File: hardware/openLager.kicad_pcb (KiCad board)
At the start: 4 copper layers, 15.2 x 19 mm, 29 parts, among them J1 CONN_01X06, J2 DM3CS-SF, U1 STM32F411CEUx, U2 SPX3819M5-L-3-3, Y1 CSTCE8M00G15L99

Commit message: Minor tweaks as per @mlyle review
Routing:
- net GND: track 80.0 -> 91.5 mm
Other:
- board text added: "5V"
- board text added: "GND"
- board text added: "NRST"
- board text added: "RX/CK"
- board text added: "SI"
- board text added: "SO"
- board text added: "TX/CS"
- board text added: "openLager Rev A ©2016 dRonin - CC BY"
- board text removed: "openLager Rev A dRonin - CC BY"

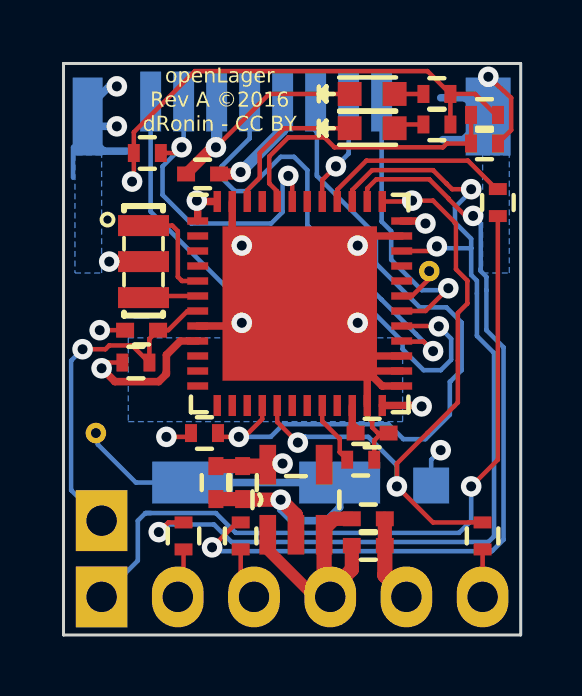
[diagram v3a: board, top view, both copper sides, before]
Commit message: DFM changes and added SS RefDes
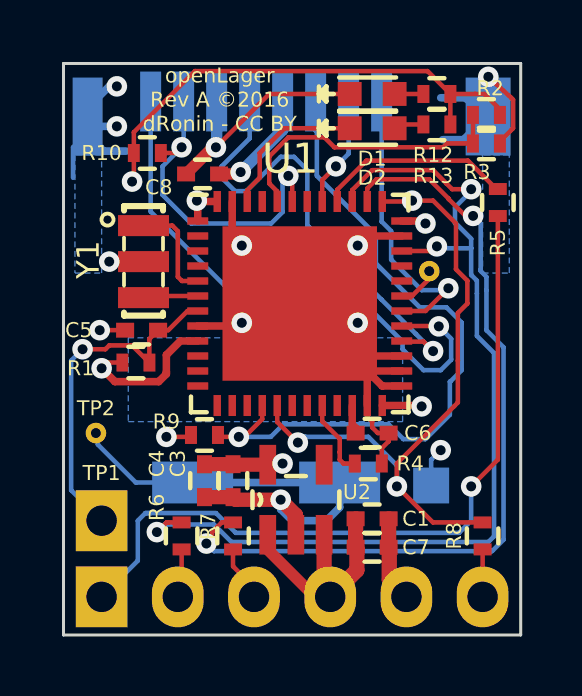
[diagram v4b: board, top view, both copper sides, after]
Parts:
- moved C4 0.39 mm to (195.2, 110.4)
- moved C3 0.32 mm to (196.2, 110.4)
- moved R4 0.28 mm to (200.7, 109.9)
- moved R7 0.25 mm to (196.2, 112.3)
- moved C7 0.14 mm to (200.8, 112.6)
- moved C1 0.13 mm to (200.8, 111.7)
- moved R2 0.06 mm to (204.6, 98.2)
- moved R3 0.06 mm to (204.6, 99.2)
- moved R9 0.06 mm to (195.2, 108.9)
- moved R6 0.06 mm to (194.4, 112.3)
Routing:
- net Net-(J1-Pad3): track 2.48 -> 1.87 mm
- net +3V3: track 31.8 -> 32.4 mm
- net GND: track 91.5 -> 92.1 mm

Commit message: Put dRonin logo on board (#42)
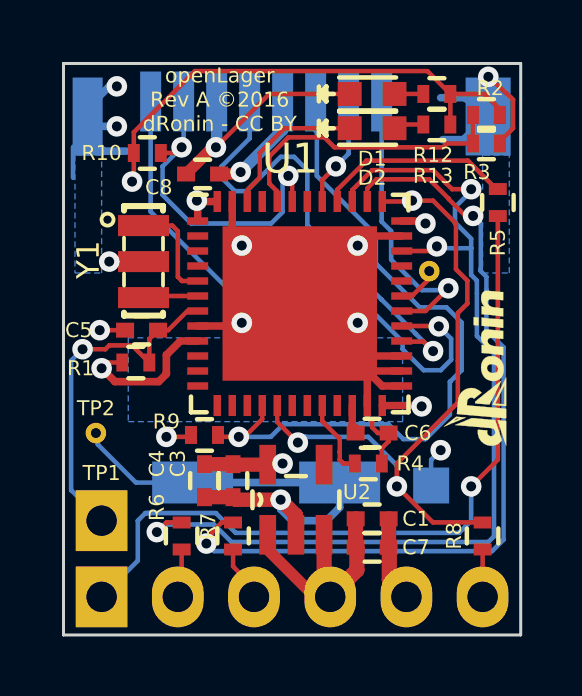
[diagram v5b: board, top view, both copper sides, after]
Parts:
- added G***: LOGO, dRLogo:test, F.Cu at (204.2, 106.7)

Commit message: Hardware rev b (#50)
* Updated to RevB, changed LED and SS

* Adding new BOM

* Changing SCH rev

* Change /NRST from pin to TP
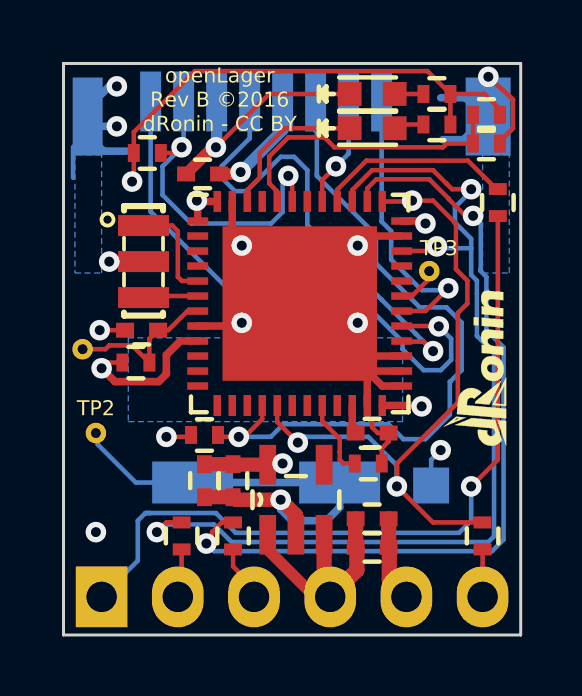
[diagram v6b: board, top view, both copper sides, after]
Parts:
- D1: value APHHS1005CGCK -> LG L29K-F2J1-24
- D2: value APHHS1005SURCK -> LS L29K-G1J2-1-Z
- TP1: footprint openLagerFootprints:Socket_Strip_Straight_1x01 -> openLagerFootprints:TP
- moved TP1 5.75 mm to (191.1, 106.0)
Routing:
- net NRST: track 12.7 -> 5.30 mm, vias 1 -> 0
- net GND: vias 12 -> 13
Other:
- board text added: "openLager Rev B ©2016 dRonin - CC BY"
- board text removed: "NRST"
- board text removed: "openLager Rev A ©2016 dRonin - CC BY"

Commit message: Add (very simple) fab drawing to openlager. (#51)
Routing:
- net GND: vias 13 -> 12
- net (no net): vias 0 -> 1
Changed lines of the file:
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@@
     (area 186.709267 94.1961 208.776305 121.981539)
     (thickness 1.6)
-    (drawings 12)
+    (drawings 16)
     (tracks 428)
     (zones 0)
@@
     (1 In1.Cu power hide)
     (2 In2.Cu power hide)
-    (31 B.Cu signal)
+    (31 B.Cu signal hide)
     (34 B.Paste user hide)
     (35 F.Paste user hide)
-    (36 B.SilkS user)
-    (37 F.SilkS user)
+    (36 B.SilkS user hide)
+    (37 F.SilkS user hide)
     (38 B.Mask user hide)
     (39 F.Mask user hide)
     (40 Dwgs.User user hide)
-    (44 Edge.Cuts user)
+    (44 Edge.Cuts user hide)
+    (49 F.Fab user)
   )
   (setup
@@
     (pcb_text_size 1.5 1.5)
     (mod_edge_width 0.15)
-    (mod_text_size 1 1)
-    (mod_text_width 0.15)
+    (mod_text_size 0.5 0.5)
+    (mod_text_width 0.125)
     (pad_size 2.2352 2.2352)
     (pad_drill 1.016)
@@
     (pad_to_paste_clearance_ratio -0.1)
     (aux_axis_origin 0 0)
-    (visible_elements 7FFFFF5F)
+    (visible_elements 7FFFFB3F)
     (pcbplotparams
       (layerselection 0x010fc_80000007)
@@
     (tags "capacitor 0402")
     (attr smd)
-    (fp_text reference C1 (at 1.4605 0) (layer F.SilkS) hide
+    (fp_text reference C1 (at 0 0) (layer F.Fab)
       (effects (font (size 0.5 0.5) (thickness 0.125)))
     )
@@
     (tags "capacitor 0402")
     (attr smd)
-    (fp_text reference C3 (at -0.5715 1.8415 270) (layer F.SilkS) hide
+    (fp_text reference C3 (at 0 0 270) (layer F.Fab)
       (effects (font (size 0.5 0.5) (thickness 0.125)))
     )
@@
     (tags "capacitor 0402")
     (attr smd)
-    (fp_text reference C4 (at -0.5715 1.5875 270) (layer F.SilkS) hide
+    (fp_text reference C4 (at 0 0 270) (layer F.Fab)
       (effects (font (size 0.5 0.5) (thickness 0.125)))
     )
@@
     (tags "capacitor 0402")
     (attr smd)
-    (fp_text reference C5 (at 2.0955 0 180) (layer F.SilkS) hide
+    (fp_text reference C5 (at 0 0 180) (layer F.Fab)
       (effects (font (size 0.5 0.5) (thickness 0.125)))
     )
@@
     (tags "capacitor 0402")
     (attr smd)
-    (fp_text reference C6 (at 1.524 0) (layer F.SilkS) hide
+    (fp_text reference C6 (at 0 0) (layer F.Fab)
       (effects (font (size 0.5 0.5) (thickness 0.125)))
     )
@@
     (tags "capacitor 0402")
     (attr smd)
-    (fp_text reference C7 (at 1.4605 0) (layer F.SilkS) hide
+    (fp_text reference C7 (at 0 0) (layer F.Fab)
       (effects (font (size 0.5 0.5) (thickness 0.125)))
     )
@@
     (tags "capacitor 0402")
     (attr smd)
-    (fp_text reference C8 (at 1.4605 -0.4445 180) (layer F.SilkS) hide
+    (fp_text reference C8 (at 0 0 180) (layer F.Fab)
       (effects (font (size 0.5 0.5) (thickness 0.125)))
     )
@@
     (attr smd)
     (fp_text reference J2 (at 1.524 -13.335) (layer B.SilkS) hide
-      (effects (font (size 1 1) (thickness 0.15)) (justify mirror))
+      (effects (font (size 0.5 0.5) (thickness 0.125)) (justify mirror))
     )
     (fp_text value DM3CS-SF (at -7.025 -16.065) (layer B.SilkS) hide
@@
     (tags "resistor 0402")
     (attr smd)
-    (fp_text reference R1 (at -1.8415 0.1905) (layer F.SilkS) hide
+    (fp_text reference R1 (at 0 0) (layer F.Fab)
       (effects (font (size 0.5 0.5) (thickness 0.125)))
     )
@@
     (tags "resistor 0402")
     (attr smd)
-    (fp_text reference R2 (at -0.127 0.889 180) (layer F.SilkS) hide
+    (fp_text reference R2 (at 0 0 180) (layer F.Fab)
       (effects (font (size 0.5 0.5) (thickness 0.125)))
     )
@@
     (tags "resistor 0402")
     (attr smd)
-    (fp_text reference R3 (at -0.3175 0.9525) (layer F.SilkS) hide
+    (fp_text reference R3 (at 0 0) (layer F.Fab)
       (effects (font (size 0.5 0.5) (thickness 0.125)))
     )
@@
     (tags "resistor 0402")
     (attr smd)
-    (fp_text reference R4 (at 1.397 0) (layer F.SilkS) hide
+    (fp_text reference R4 (at 0 0) (layer F.Fab)
       (effects (font (size 0.5 0.5) (thickness 0.125)))
     )
@@
     (tags "resistor 0402")
     (attr smd)
-    (fp_text reference R5 (at -1.3335 0 90) (layer F.SilkS) hide
+    (fp_text reference R5 (at 0 0 90) (layer F.Fab)
       (effects (font (size 0.5 0.5) (thickness 0.125)))
     )
@@
     (tags "resistor 0402")
     (attr smd)
-    (fp_text reference R6 (at 0.9525 -0.8255 90) (layer F.SilkS) hide
+    (fp_text reference R6 (at 0 0 90) (layer F.Fab)
       (effects (font (size 0.5 0.5) (thickness 0.125)))
     )
@@
     (tags "resistor 0402")
     (attr smd)
-    (fp_text reference R7 (at 0.3175 -0.8255 90) (layer F.SilkS) hide
+    (fp_text reference R7 (at 0 0 90) (layer F.Fab)
       (effects (font (size 0.5 0.5) (thickness 0.125)))
     )
@@
     (tags "resistor 0402")
     (attr smd)
-    (fp_text reference R8 (at 0 -0.9525 90) (layer F.SilkS) hide
+    (fp_text reference R8 (at 0 0 90) (layer F.Fab)
       (effects (font (size 0.5 0.5) (thickness 0.125)))
     )
@@
     (tags "resistor 0402")
     (attr smd)
-    (fp_text reference R9 (at -1.27 -0.4445) (layer F.SilkS) hide
+    (fp_text reference R9 (at 0 0) (layer F.Fab)
       (effects (font (size 0.5 0.5) (thickness 0.125)))
     )
@@
     (tags "resistor 0402")
     (attr smd)
-    (fp_text reference R10 (at -1.524 0) (layer F.SilkS) hide
+    (fp_text reference R10 (at 0 0) (layer F.Fab)
       (effects (font (size 0.5 0.5) (thickness 0.125)))
     )
@@
     (tags "resistor 0402")
     (attr smd)
-    (fp_text reference R12 (at -0.127 2.032) (layer F.SilkS) hide
+    (fp_text reference R12 (at 0 0) (layer F.Fab)
       (effects (font (size 0.5 0.5) (thickness 0.125)))
     )
@@
     (tags "resistor 0402")
     (attr smd)
-    (fp_text reference R13 (at 0.127 -1.7145 180) (layer F.SilkS) hide
+    (fp_text reference R13 (at 0 0 180) (layer F.Fab)
       (effects (font (size 0.5 0.5) (thickness 0.125)))
     )
@@
     (tags "QFN 0.5")
     (attr smd)
-    (fp_text reference U1 (at -0.3175 -4.826) (layer F.SilkS) hide
-      (effects (font (size 1 1) (thickness 0.15)))
+    (fp_text reference U1 (at 0 0) (layer F.Fab)
+      (effects (font (size 0.5 0.5) (thickness 0.125)))
     )
     (fp_text value STM32F411CEUx (at 0 4.75) (layer F.Fab) hide
@@
     (solder_mask_margin 0.1)
     (attr smd)
-    (fp_text reference Y1 (at -0.0635 1.8415 270) (layer F.SilkS) hide
-      (effects (font (size 0.75 0.75) (thickness 0.1)))
+    (fp_text reference Y1 (at 0 0 270) (layer F.Fab)
+      (effects (font (size 0.5 0.5) (thickness 0.125)))
     )
     (fp_text value CSTCE8M00G15L99 (at 0.3175 1.8875 270) (layer F.SilkS) hide
@@
     (tags "socket strip")
     (fp_text reference J1 (at 0 -5.1) (layer F.SilkS) hide
-      (effects (font (size 1 1) (thickness 0.15)))
+      (effects (font (size 0.5 0.5) (thickness 0.125)))
     )
     (fp_text value CONN_01X06 (at 0 -3.1) (layer F.Fab) hide
@@
     (tags "LED led 0603 SMD smd SMT smt smdled SMDLED smtled SMTLED")
     (attr smd)
-    (fp_text reference D1 (at 0 2.159) (layer F.SilkS) hide
+    (fp_text reference D1 (at 0 0) (layer F.Fab)
       (effects (font (size 0.5 0.5) (thickness 0.125)))
     )
@@
     (tags "LED led 0603 SMD smd SMT smt smdled SMDLED smtled SMTLED")
     (attr smd)
-    (fp_text reference D2 (at 0 1.651) (layer F.SilkS) hide
+    (fp_text reference D2 (at 0 0) (layer F.Fab)
       (effects (font (size 0.5 0.5) (thickness 0.125)))
     )
@@
     (solder_mask_margin 0.1)
     (attr smd)
-    (fp_text reference U2 (at 0.254 2.032 180) (layer F.SilkS) hide
+    (fp_text reference U2 (at 0 0 180) (layer F.Fab)
       (effects (font (size 0.5 0.5) (thickness 0.125)))
     )
@@
     (at 204.216 106.68 90)
     (fp_text reference G*** (at 0 0 90) (layer F.SilkS) hide
-      (effects (font (thickness 0.3)))
+      (effects (font (size 0.5 0.5) (thickness 0.125)))
     )
     (fp_text value LOGO (at 0.75 0 90) (layer F.SilkS) hide
@@
     (at 191.135 106.045)
     (fp_text reference TP1 (at 0 0.5) (layer F.SilkS) hide
-      (effects (font (size 1 1) (thickness 0.15)))
+      (effects (font (size 0.5 0.5) (thickness 0.125)))
     )
     (fp_text value TEST_1P (at 0 -0.5) (layer F.Fab) hide
@@
       (net 4 NRST))
   )
+  (gr_line (start 199.39 98.425) (end 199.39 98.933) (angle 90) (layer F.Fab) (width 0.2))
+  (gr_line (start 199.39 97.282) (end 199.39 97.79) (angle 90) (layer F.Fab) (width 0.2))
+  (gr_circle (center 197.104 111.252) (end 197.104 111.125) (layer F.Fab) (width 0.2))
+  (gr_circle (center 195.58 101.727) (end 195.58 101.6) (layer F.Fab) (width 0.2))
   (gr_text SI (at 204.47 112.649) (layer B.SilkS)
     (effects (font (size 0.5 0.5) (thickness 0.1)) (justify mirror))
@@
   (gr_line (start 205.74 115.57) (end 205.74 96.52) (angle 90) (layer Edge.Cuts) (width 0.1))
   (gr_line (start 190.5 115.57) (end 205.74 115.57) (angle 90) (layer Edge.Cuts) (width 0.1))
+  (via (at 191.5795 112.141) (size 0.6858) (drill 0.3302) (layers F.Cu B.Cu) (net 0))
   (segment (start 200.237 111.6965) (end 200.237 112.649) (width 0.508) (layer F.Cu) (net 1))
   (segment (start 200.237 112.649) (end 200.279 112.691) (width 0.508) (layer F.Cu) (net 1))
@@
   (segment (start 199.1868 112.1664) (end 199.1868 112.0267) (width 0.508) (layer F.Cu) (net 1))
   (segment (start 199.1868 114.0968) (end 199.39 114.3) (width 0.508) (layer F.Cu) (net 1))
-  (via (at 191.5795 112.141) (size 0.6858) (drill 0.3302) (layers F.Cu B.Cu) (net 2))
   (segment (start 197.739 111.0615) (end 196.2365 111.0615) (width 0.47625) (layer F.Cu) (net 2))
   (segment (start 196.2365 111.0615) (end 196.1515 110.9765) (width 0.47625) (layer F.Cu) (net 2))
